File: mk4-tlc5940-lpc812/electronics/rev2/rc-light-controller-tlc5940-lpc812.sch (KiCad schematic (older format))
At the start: 42 parts, among them T1 NMOSSOT23, U2 TLC5940PWP

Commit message: Change LPC footprint
NEED TO VERIFY IT IS THE CORRECT ONE!
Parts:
- U$2: footprint rc-light-controller-tlc5940-lpc812:TSSOP16 -> Package_SO:SSOP-16_4.4x5.2mm_P0.65mm
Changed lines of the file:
@@
 F 0 "U$2" H 6900 4500 42  0000 L BNN
 F 1 "LPC812" H 7800 5200 50  0001 C CNN
-F 2 "rc-light-controller-tlc5940-lpc812:TSSOP16" H 7800 5200 50  0001 C CNN
+F 2 "Package_SO:SSOP-16_4.4x5.2mm_P0.65mm" H 7800 5200 50  0001 C CNN
 F 3 "" H 7800 5200 50  0001 C CNN
 	1    7800 5200

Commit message: Fix LPC812 footprint
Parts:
- U$2: footprint Package_SO:SSOP-16_4.4x5.2mm_P0.65mm -> Package_SO:TSSOP-16_4.4x5mm_P0.65mm
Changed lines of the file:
@@
 F 0 "U$2" H 6900 4500 42  0000 L BNN
 F 1 "LPC812" H 7800 5200 50  0001 C CNN
-F 2 "Package_SO:SSOP-16_4.4x5.2mm_P0.65mm" H 7800 5200 50  0001 C CNN
+F 2 "Package_SO:TSSOP-16_4.4x5mm_P0.65mm" H 7800 5200 50  0001 C CNN
 F 3 "" H 7800 5200 50  0001 C CNN
 	1    7800 5200

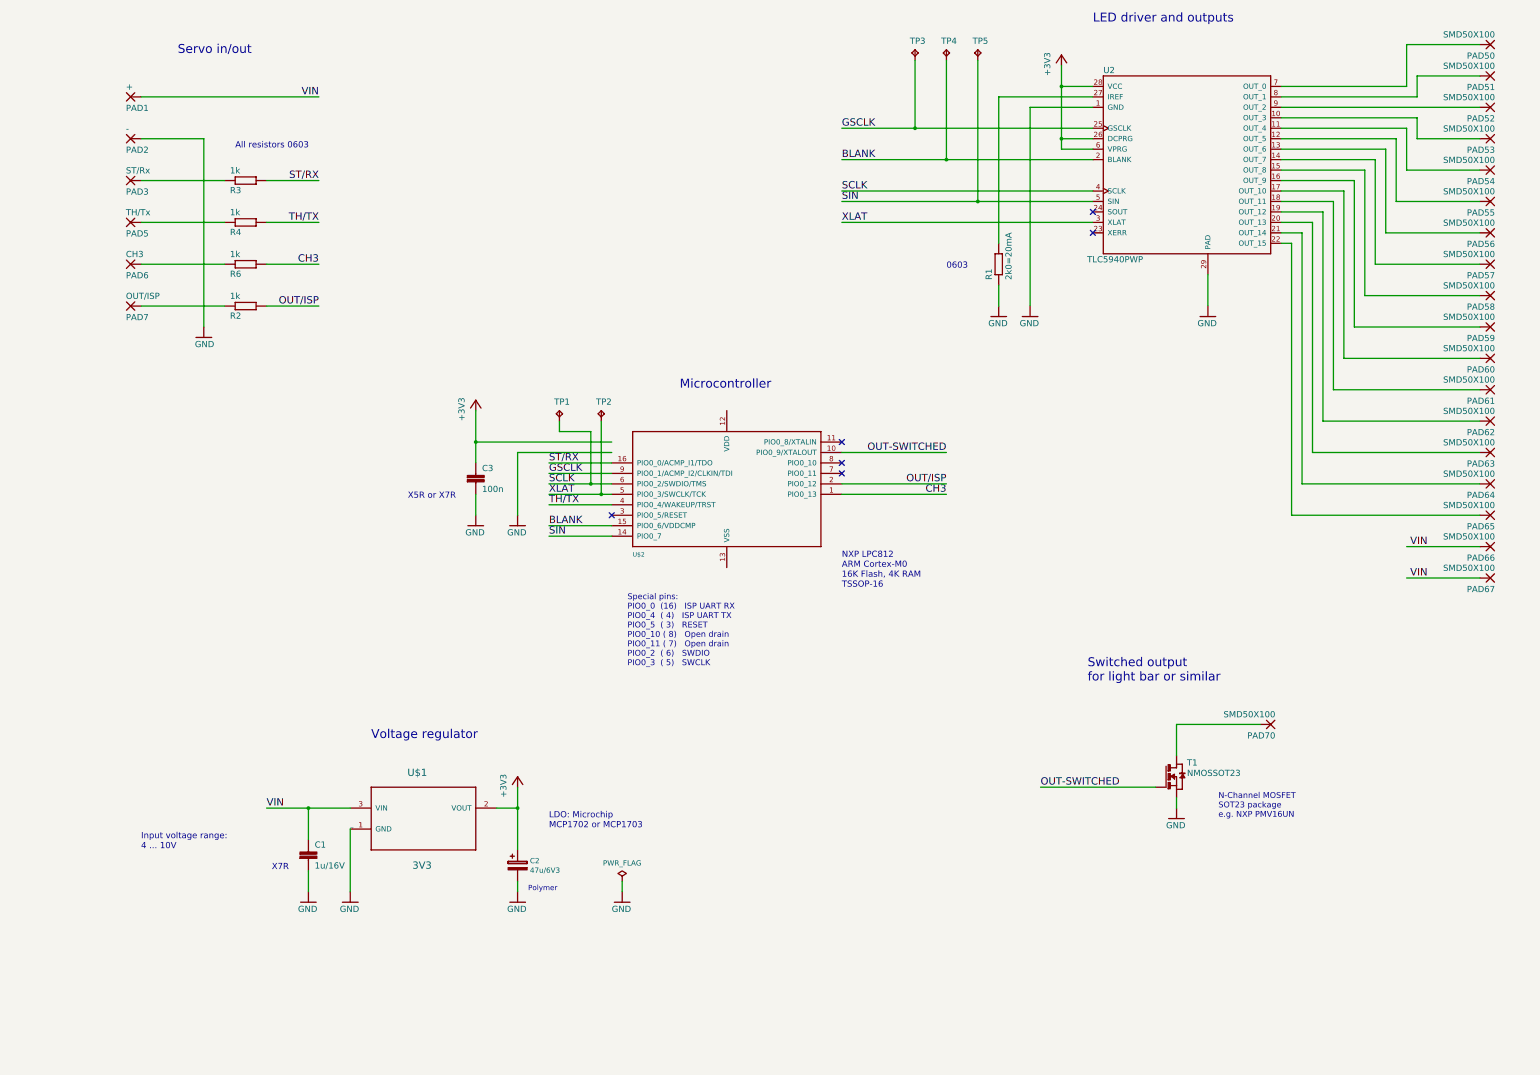
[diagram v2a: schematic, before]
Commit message: Improve schematics and rename references
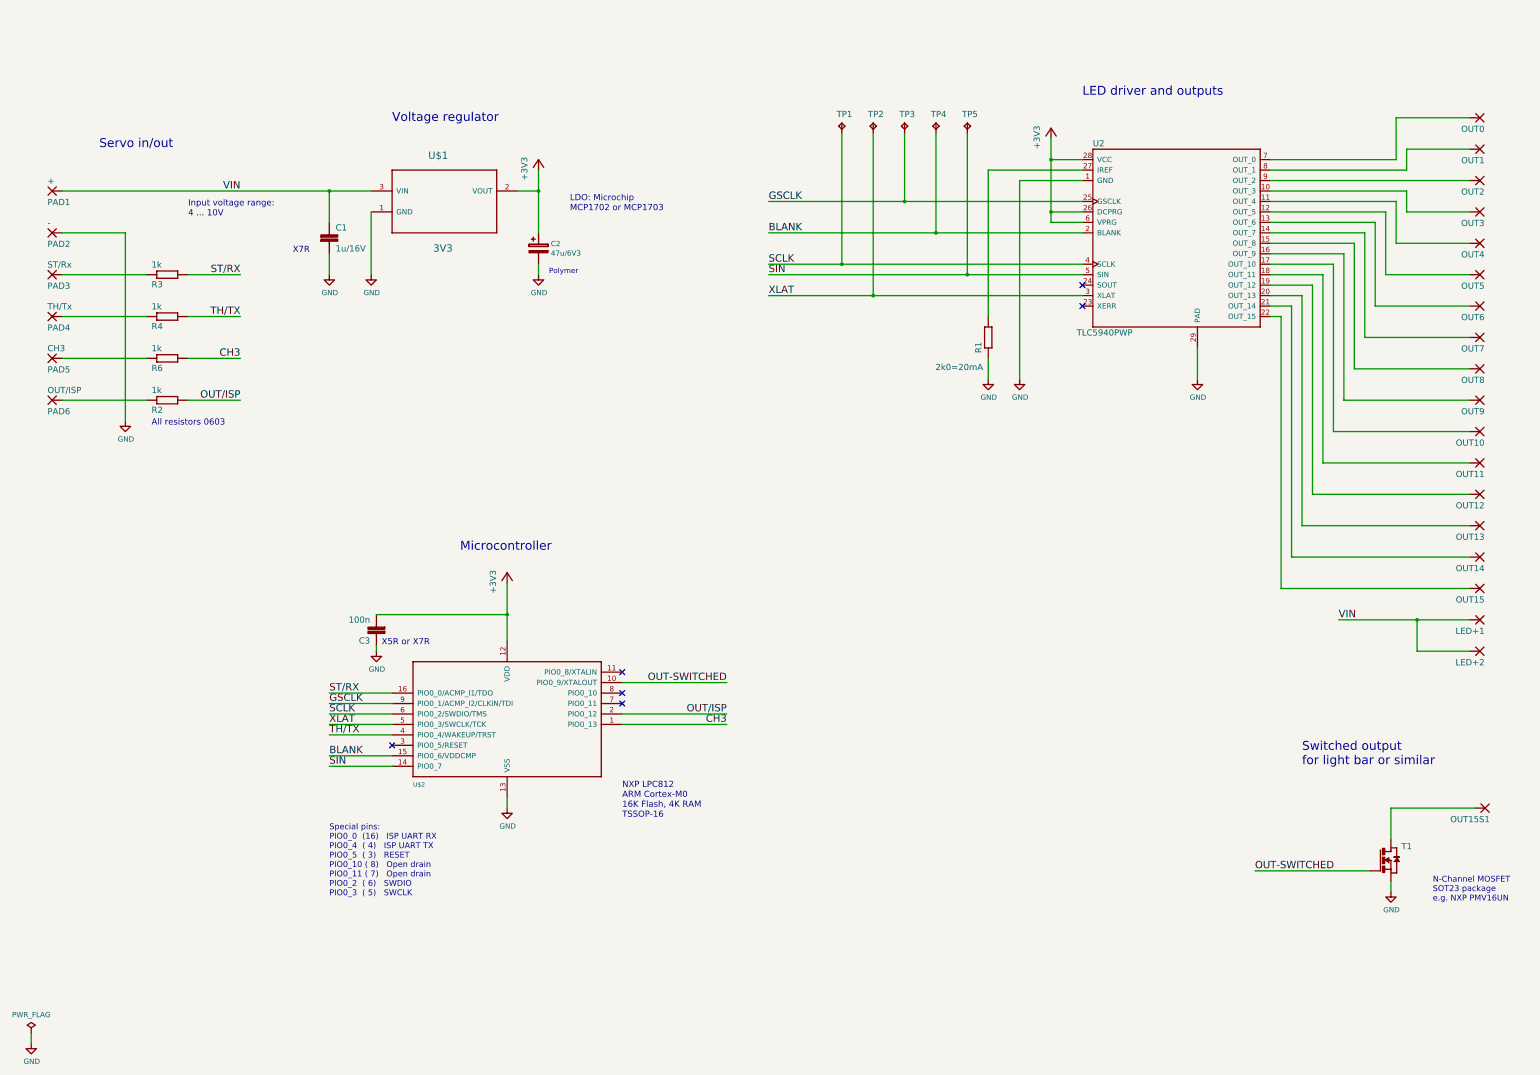
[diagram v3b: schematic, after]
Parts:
- renumbered PAD66 to LED+1, PAD67 to LED+2, PAD50 to OUT0, PAD51 to OUT1, PAD60 to OUT10, PAD61 to OUT11, PAD62 to OUT12, PAD63 to OUT13, PAD64 to OUT14, PAD65 to OUT15, PAD70 to OUT15S1, PAD52 to OUT2, PAD53 to OUT3, PAD54 to OUT4, PAD55 to OUT5, PAD56 to OUT6, PAD57 to OUT7, PAD58 to OUT8, PAD59 to OUT9, PAD5 to PAD4, PAD6 to PAD5, PAD7 to PAD6
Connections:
- wire segments 118 -> 116
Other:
- note removed: "0603"
- moved on the sheet: C1, C2, C3, LED+1, LED+2, OUT0, OUT1, OUT10, OUT11, OUT12, OUT13, OUT14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
